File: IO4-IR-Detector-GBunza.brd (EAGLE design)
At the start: 99.1 x 66 mm, 45 parts, among them CON2 IO4INV, IC1 TL331, IC2 TL331, IC3 TL331, IC4 TL331, Q1 2N7002, Q2 2N7002, Q3 2N7002, Q4 2N7002

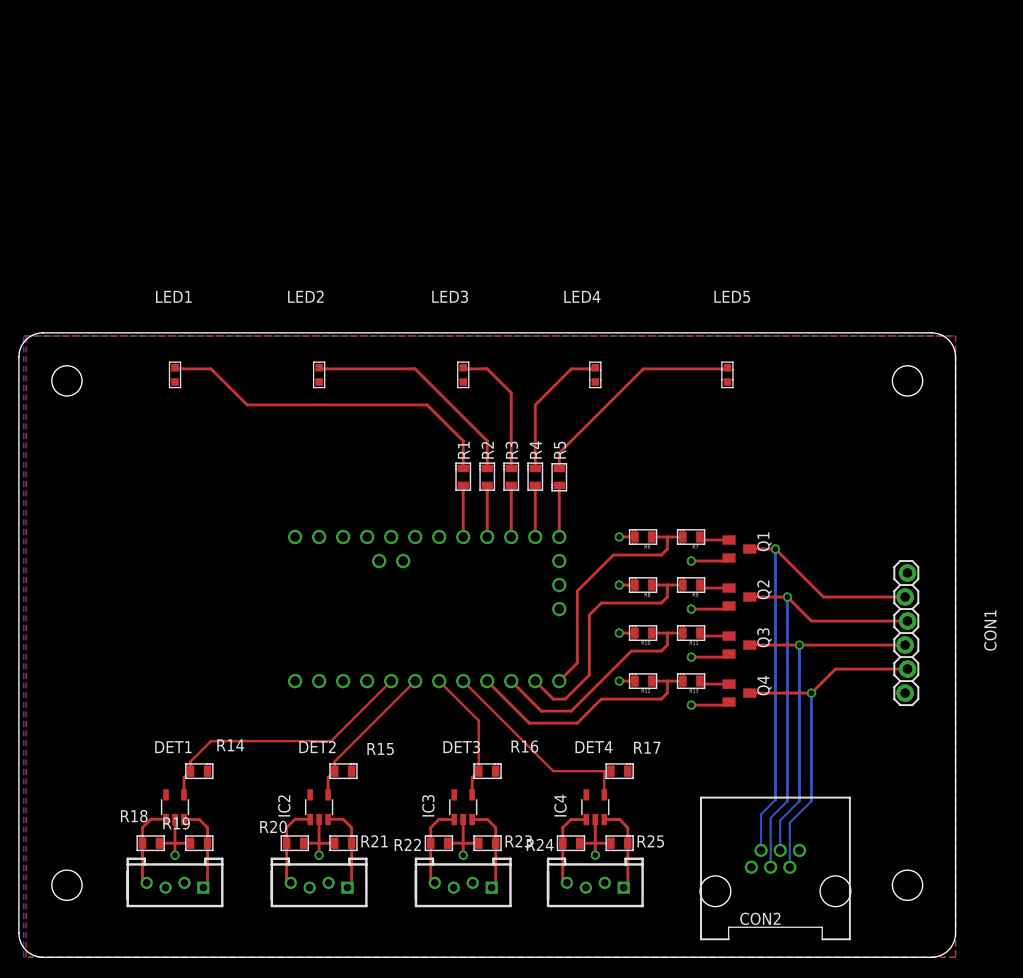
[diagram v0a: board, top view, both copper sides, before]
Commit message: changed from expensive TL331 to inexpensive LM258/LM358
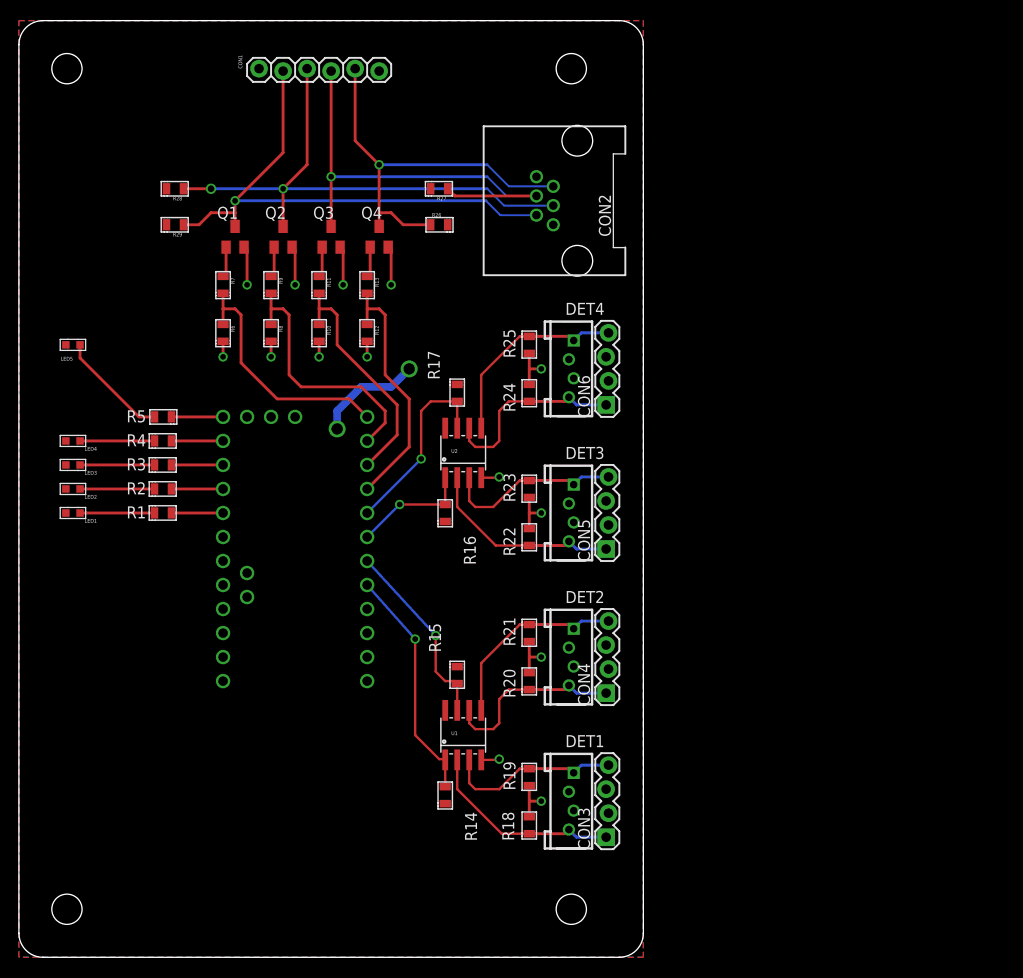
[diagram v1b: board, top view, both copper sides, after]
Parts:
- removed IC1, IC2, IC3, IC4: TL331, SPCoast:SOT-23-5
- added CON3, CON4, CON5, CON6: (no value), SPCoast:1X04_LOCK
- added R26, R27, R28, R29: 10K, SPCoast:0805-RES
- added U1, U2: LM393M, SPCoast:SO08
- moved CON1 86.9 mm to (25.4, 94.0), turned to 0 degrees
- moved CON2 76.0 mm to (59.1, 80.0), turned to 90 degrees
- moved LED5 69.3 mm to (5.71, 64.8), turned to 0 degrees
- moved Q1 62.7 mm to (22.9, 76.2), turned to 0 degrees
- moved Q2 61.5 mm to (27.9, 76.2), turned to 0 degrees
- moved Q4 61.5 mm to (38.1, 76.2), turned to 0 degrees
- moved Q3 61.1 mm to (33.0, 76.2), turned to 0 degrees
- moved R7 56.3 mm to (21.6, 71.1), turned to 270 degrees
- moved LED4 55.7 mm to (5.71, 54.6), turned to 0 degrees
- moved DET4 54.7 mm to (58.4, 62.2), turned to 270 degrees
- moved R9 54.6 mm to (26.7, 71.1), turned to 270 degrees
- moved R13 54.2 mm to (36.8, 71.1), turned to 270 degrees
- moved R11 53.9 mm to (31.8, 71.1), turned to 270 degrees
- moved R25 53.6 mm to (54.0, 64.8), turned to 90 degrees
- moved R6 49.4 mm to (21.6, 66.0), turned to 270 degrees
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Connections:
- net DET1: now also U1.1; no longer IC1.4
- net DET2: now also U1.7; no longer IC2.4
- net DET3: now also U2.1; no longer IC3.4
- net DET4: now also U2.7; no longer IC4.4
- net GND: now also U1.4, U2.4; no longer IC1.2, IC2.2, IC3.2, IC4.2
- net N$10: now also CON4.1, U1.6; no longer IC2.1
- net N$12: now also CON4.4, U1.5; no longer IC2.3
- net N$13: now also CON5.1, U2.2; no longer IC3.1
- net N$14: now also CON5.4, U2.3; no longer IC3.3
- net N$15: now also CON6.1, U2.6; no longer IC4.1
- net N$16: now also CON6.4, U2.5; no longer IC4.3
- net N$19: now also CON3.4, U1.3; no longer IC1.3
- net N$9: now also CON3.1, U1.2; no longer IC1.1
- net OD1: now also R26.1
- net OD2: now also R27.1
- net OD3: now also R28.1
- net OD4: now also R29.1
- net VCC: now also CON3.2, CON3.3, CON4.2, CON4.3, CON5.2, CON5.3, CON6.2, CON6.3, R26.2, R27.2, R28.2, R29.2, U1.8, U2.8; no longer IC1.5, IC2.5, IC3.5, IC4.5
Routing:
- net N$7: track 36.6 -> 7.88 mm
- net N$4: track 23.9 -> 7.88 mm
- net N$9: track 8.89 -> 21.3 mm
- net N$13: track 8.86 -> 21.1 mm
- net N$16: track 9.37 -> 21.3 mm
- net N$15: track 8.86 -> 20.5 mm
- net VCC: track 0.00 -> 11.4 mm, vias 0 -> 2
- net N$1: track 23.1 -> 11.8 mm
- net N$12: track 9.40 -> 20.7 mm
- net N$10: track 8.89 -> 19.8 mm
- net OD3: track 47.0 -> 57.6 mm, vias 1 -> 2
- net N$14: track 9.37 -> 19.1 mm
- net OD2: track 39.0 -> 48.7 mm
- net N$19: track 9.37 -> 18.9 mm
- net N$2: track 14.7 -> 7.88 mm
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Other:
- board size 99.1 x 66 mm -> 66 x 99.1 mm
- board text added: "!DETECTED! Open Drain outputs"
- board text added: "... is dimmer than"
- board text added: "2020.09"
- board text added: "Activity"
- board text added: "Ambient (in open area)"
- board text added: "Detect (under train)"
- board text added: "Detector triggers when ..."
- board text added: "EA+ +DE"
- board text added: "Use with PT19-21C/L41 Photodetector "Fingers""
- board text added: "v4.0"
- board text removed: "2018-02"
- board text removed: "Ambient"
- board text removed: "Detect"
- board text removed: "E + + E"
- board text removed: "PT19-21C/L41 Photodetector"
- board text removed: "v3.2"

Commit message: added V4 changes note to sch
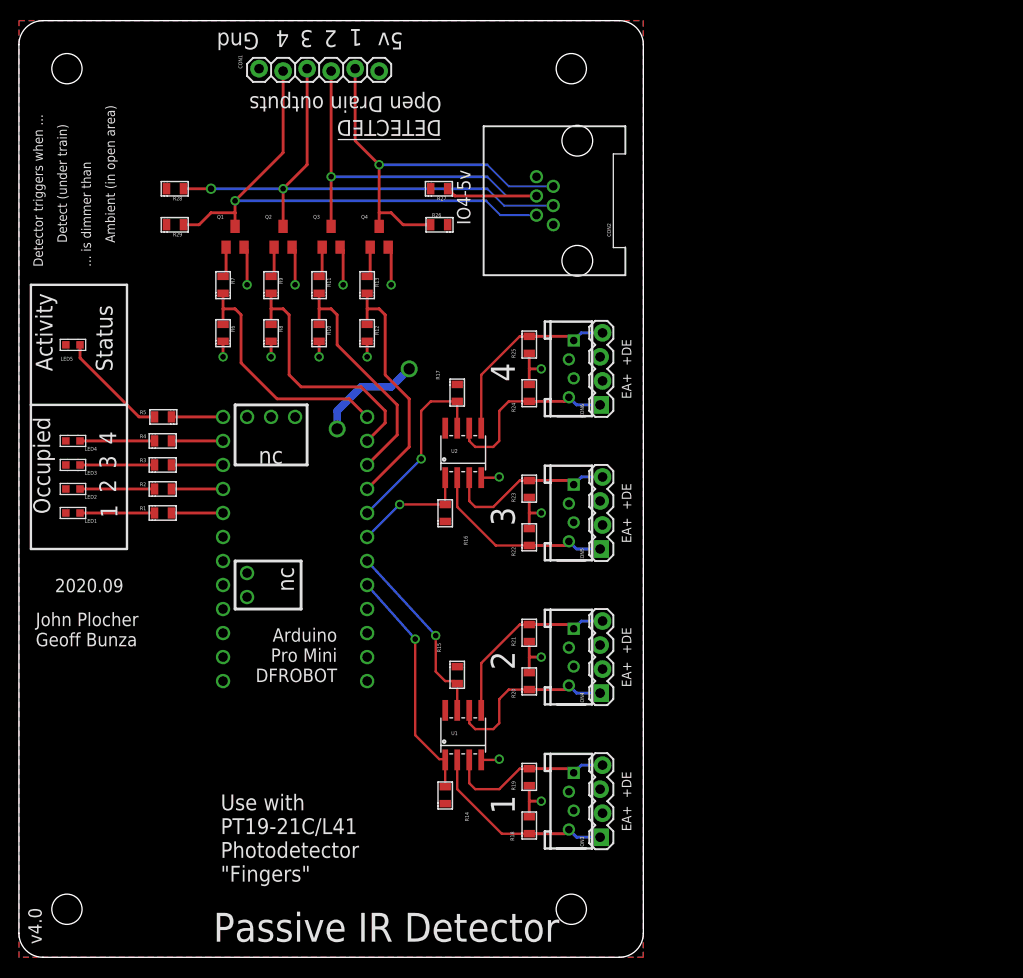
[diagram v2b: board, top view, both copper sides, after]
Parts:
- moved CON3 0.63 mm to (61.6, 12.7)
- moved CON4 0.63 mm to (61.6, 27.9)
- moved CON5 0.63 mm to (61.6, 43.2)
- moved CON6 0.63 mm to (61.6, 58.4)
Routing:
- net N$9: track 21.3 -> 20.7 mm
- net N$19: track 18.9 -> 18.2 mm
- net N$16: track 21.3 -> 20.7 mm
- net N$15: track 20.5 -> 19.8 mm
- net N$14: track 19.1 -> 18.5 mm
- net N$13: track 21.1 -> 20.4 mm
- net N$12: track 20.7 -> 20.0 mm
- net N$10: track 19.8 -> 19.2 mm

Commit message: op-amp value changed to LM358B
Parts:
- U1: value LM393M -> LM358B
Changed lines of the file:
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@@
 <attribute name="VALUE" x="18.923" y="67.056" size="1.016" layer="27" font="vector" rot="R270"/>
 </element>
-<element name="U1" library="SPCoast" package="SO08" value="LM393M" x="46.99" y="23.495" smashed="yes">
+<element name="U1" library="SPCoast" package="SO08" value="LM358B" x="46.99" y="23.495" smashed="yes">
 <attribute name="VALUE" x="45.72" y="22.86" size="0.4064" layer="27"/>
 <attribute name="NAME" x="45.72" y="23.495" size="0.4064" layer="25"/>

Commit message: normalized values
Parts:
- ARDUINO1: value ARDUINO-PRO-MINI-DAVESROBOT -> DAVEK
- CON1, CON4, CON5, CON6: value (none) -> 0.100
- CON2: value IO4INV -> RJ12/6
- CON3: value (none) -> 2mm
- DET1, DET2, DET3, DET4: value CONNECTOR-GROVE-4P-2.0-3470130P1 -> 2mm
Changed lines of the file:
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@@
 <attribute name="VALUE" x="44.6405" y="15.113" size="0.4064" layer="27" font="vector" rot="R270"/>
 </element>
-<element name="CON2" library="SPCoast" package="RJ25-INVERTED" value="IO4INV" x="59.055" y="80.01" smashed="yes" rot="R90">
+<element name="CON2" library="SPCoast" package="RJ25-INVERTED" value="RJ12/6" x="59.055" y="80.01" smashed="yes" rot="R90">
 <attribute name="NAME" x="62.611" y="76.2" size="0.4064" layer="25" font="vector" rot="R90"/>
 </element>
-<element name="ARDUINO1" library="SPCoast" package="ARDUINO_PRO_MINI_DAVEK" value="ARDUINO-PRO-MINI-DAVESROBOT" x="38.1" y="58.42" smashed="yes" rot="R180"/>
+<element name="ARDUINO1" library="SPCoast" package="ARDUINO_PRO_MINI_DAVEK" value="DAVEK" x="38.1" y="58.42" smashed="yes" rot="R180"/>
 <element name="LED4" library="SPCoast" package="0603-LED" value="Y" x="5.715" y="54.61" smashed="yes">
 <attribute name="NAME" x="8.255" y="53.975" size="0.4064" layer="25" font="vector" rot="R180"/>
@@
 <attribute name="VALUE" x="14.478" y="61.976" size="0.4064" layer="27" font="vector" rot="R270"/>
 </element>
-<element name="CON1" library="SPCoast" package="1X06_LOCK" value="" x="25.4" y="93.98" smashed="yes">
+<element name="CON1" library="SPCoast" package="1X06_LOCK" value="0.100" x="25.4" y="93.98" smashed="yes">
 <attribute name="NAME" x="23.622" y="93.98" size="0.4064" layer="25" font="vector" rot="R90"/>
 <attribute name="VALUE" x="24.13" y="90.678" size="1.27" layer="27" font="vector"/>
 </element>
-<element name="DET1" library="SPCoast" package="4P-2.0" value="CONNECTOR-GROVE-4P-2.0-3470130P1" x="58.42" y="16.51" smashed="yes" rot="R270"/>
+<element name="DET1" library="SPCoast" package="4P-2.0" value="2mm" x="58.42" y="16.51" smashed="yes" rot="R270"/>
 <element name="R20" library="SPCoast" package="0805-RES" value="10K" x="53.975" y="29.21" smashed="yes" rot="R270">
 <attribute name="NAME" x="52.5145" y="27.432" size="0.4064" layer="25" font="vector" rot="R90"/>
@@
 <attribute name="VALUE" x="46.7995" y="32.004" size="0.4064" layer="27" font="vector" rot="R90"/>
 </element>
-<element name="DET2" library="SPCoast" package="4P-2.0" value="CONNECTOR-GROVE-4P-2.0-3470130P1" x="58.42" y="31.75" smashed="yes" rot="R270"/>
+<element name="DET2" library="SPCoast" package="4P-2.0" value="2mm" x="58.42" y="31.75" smashed="yes" rot="R270"/>
 <element name="R22" library="SPCoast" package="0805-RES" value="10K" x="53.975" y="44.45" smashed="yes" rot="R270">
 <attribute name="NAME" x="52.5145" y="42.418" size="0.4064" layer="25" font="vector" rot="R90"/>
@@
 <attribute name="VALUE" x="44.6405" y="44.831" size="0.4064" layer="27" font="vector" rot="R270"/>
 </element>
-<element name="DET3" library="SPCoast" package="4P-2.0" value="CONNECTOR-GROVE-4P-2.0-3470130P1" x="58.42" y="46.99" smashed="yes" rot="R270"/>
+<element name="DET3" library="SPCoast" package="4P-2.0" value="2mm" x="58.42" y="46.99" smashed="yes" rot="R270"/>
 <element name="R24" library="SPCoast" package="0805-RES" value="10K" x="53.975" y="59.69" smashed="yes" rot="R270">
 <attribute name="NAME" x="52.5145" y="57.658" size="0.4064" layer="25" font="vector" rot="R90"/>
@@
 <attribute name="VALUE" x="46.7995" y="61.849" size="0.4064" layer="27" font="vector" rot="R90"/>
 </element>
-<element name="DET4" library="SPCoast" package="4P-2.0" value="CONNECTOR-GROVE-4P-2.0-3470130P1" x="58.42" y="62.23" smashed="yes" rot="R270"/>
+<element name="DET4" library="SPCoast" package="4P-2.0" value="2mm" x="58.42" y="62.23" smashed="yes" rot="R270"/>
 <element name="LED5" library="SPCoast" package="0603-LED" value="Y" x="5.715" y="64.77" smashed="yes">
 <attribute name="NAME" x="5.715" y="63.5" size="0.4064" layer="25" font="vector" rot="R180"/>
@@
 <attribute name="VALUE" x="17.526" y="78.867" size="0.4064" layer="27" rot="R180"/>
 </element>
-<element name="CON3" library="SPCoast" package="1X04_LOCK" value="" x="61.595" y="12.7" smashed="yes" rot="R90">
+<element name="CON3" library="SPCoast" package="1X04_LOCK" value="2mm" x="61.595" y="12.7" smashed="yes" rot="R90">
 <attribute name="NAME" x="59.7662" y="11.3538" size="0.4064" layer="25" ratio="10" rot="R90"/>
 <attribute name="VALUE" x="64.77" y="11.43" size="1.27" layer="27" rot="R90"/>
 </element>
-<element name="CON4" library="SPCoast" package="1X04_LOCK" value="" x="61.595" y="27.94" smashed="yes" rot="R90">
+<element name="CON4" library="SPCoast" package="1X04_LOCK" value="0.100" x="61.595" y="27.94" smashed="yes" rot="R90">
 <attribute name="NAME" x="59.7662" y="26.5938" size="0.4064" layer="25" ratio="10" rot="R90"/>
 <attribute name="VALUE" x="64.77" y="26.67" size="1.27" layer="27" rot="R90"/>
 </element>
-<element name="CON5" library="SPCoast" package="1X04_LOCK" value="" x="61.595" y="43.18" smashed="yes" rot="R90">
+<element name="CON5" library="SPCoast" package="1X04_LOCK" value="0.100" x="61.595" y="43.18" smashed="yes" rot="R90">
 <attribute name="NAME" x="59.7662" y="41.8338" size="0.4064" layer="25" ratio="10" rot="R90"/>
 <attribute name="VALUE" x="64.77" y="41.91" size="1.27" layer="27" rot="R90"/>
 </element>
-<element name="CON6" library="SPCoast" package="1X04_LOCK" value="" x="61.595" y="58.42" smashed="yes" rot="R90">
+<element name="CON6" library="SPCoast" package="1X04_LOCK" value="0.100" x="61.595" y="58.42" smashed="yes" rot="R90">
 <attribute name="NAME" x="59.7662" y="57.0738" size="0.4064" layer="25" ratio="10" rot="R90"/>
 <attribute name="VALUE" x="64.77" y="57.15" size="1.27" layer="27" rot="R90"/>

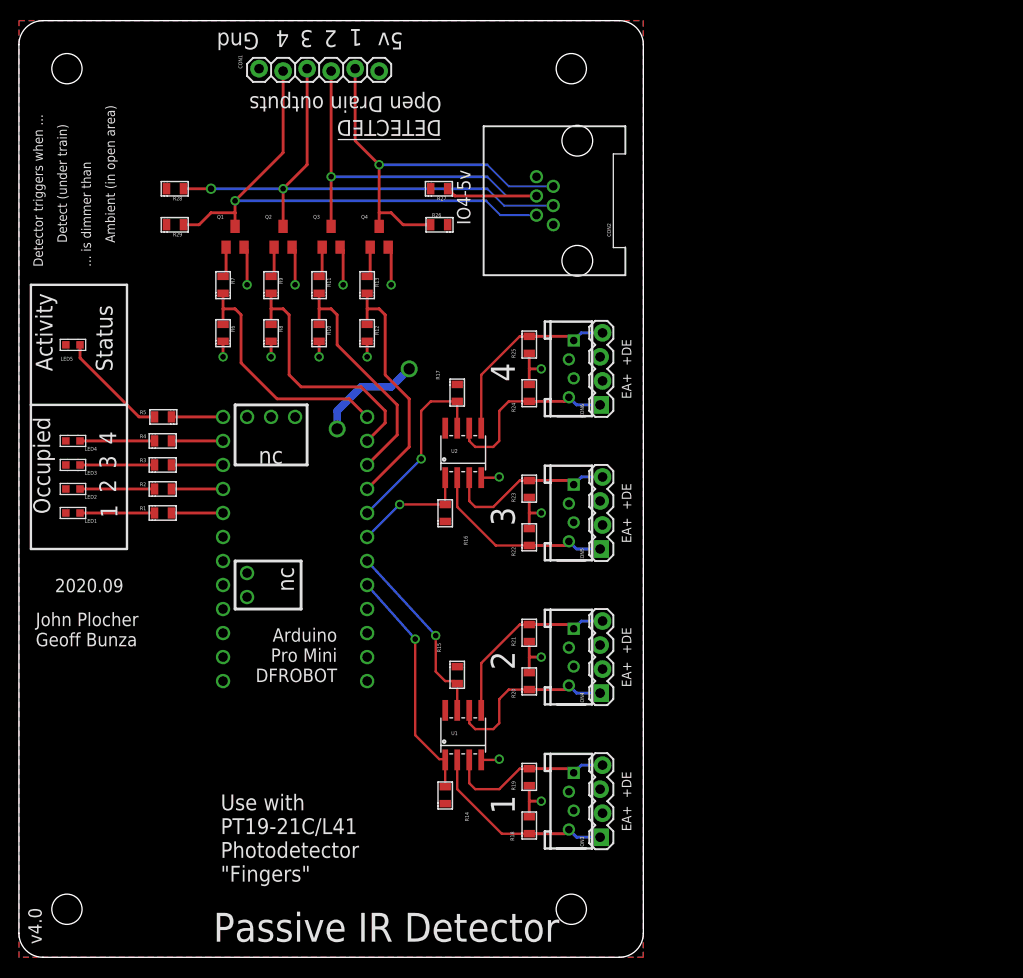
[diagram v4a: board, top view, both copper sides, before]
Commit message: Vscore changed to mouse bites, larger
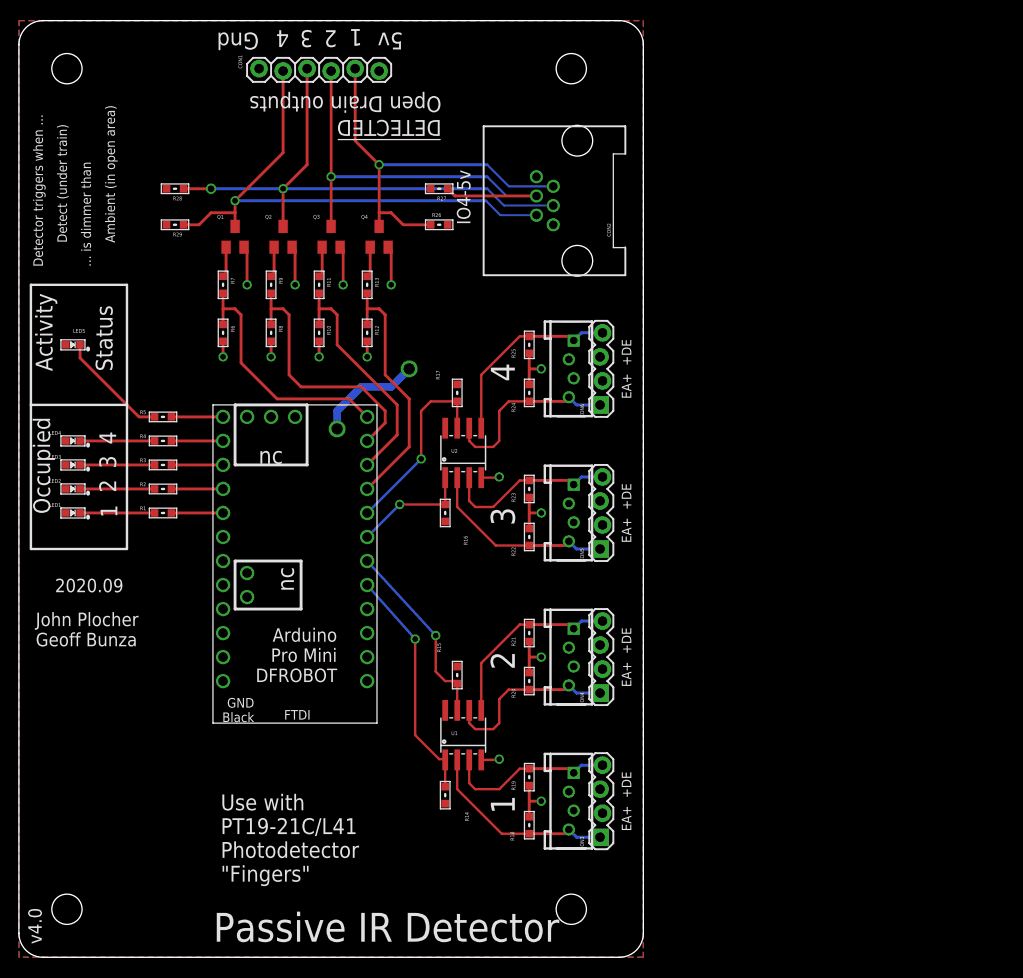
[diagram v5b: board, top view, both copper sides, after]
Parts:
- R1, R10, R11, R12, R13, R14, R15, R16, R17, R18, R19, R2, R20, R21, R22, R23, R24, R25, R26, R27, R28, R29, R3, R4, R5, R6, R7, R8, R9: device SPCoast:0805-RES -> SPCoast:0603-RES
- turned LED1 to 180 degrees
- turned LED2 to 180 degrees
- turned LED3 to 180 degrees
- turned LED4 to 180 degrees
- turned LED5 to 180 degrees
